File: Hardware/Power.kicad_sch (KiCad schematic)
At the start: 17 parts

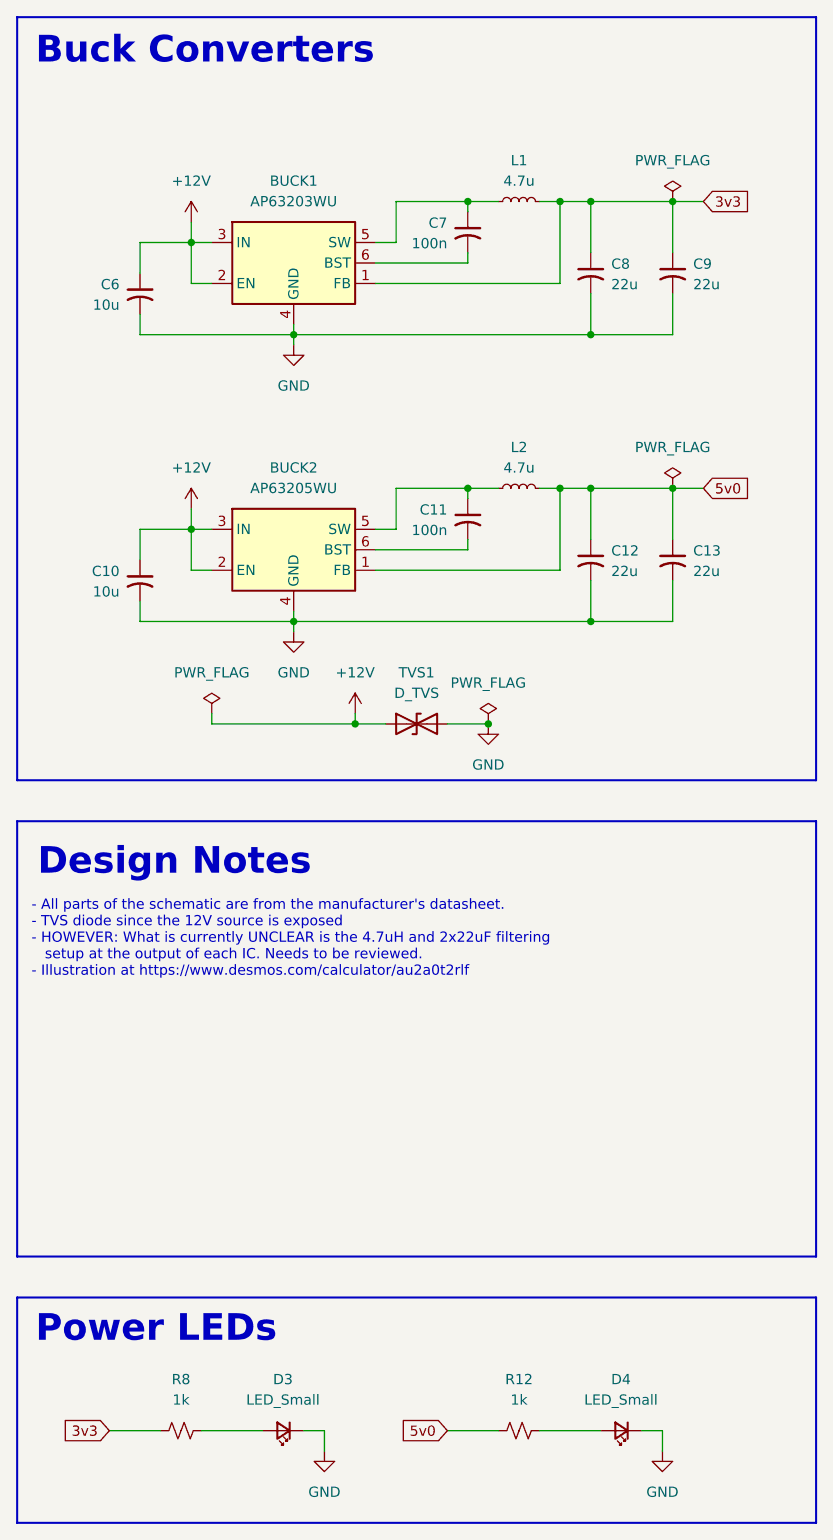
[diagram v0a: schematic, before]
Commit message: Fixed up the schematic a little, and did *most* footprint assigning
- Most footprints are assigned. Ones that arent either don't exist, or
  are out of stock at digikey and are thus not work making/adding.
- Details of next steps will be put into changelog soon
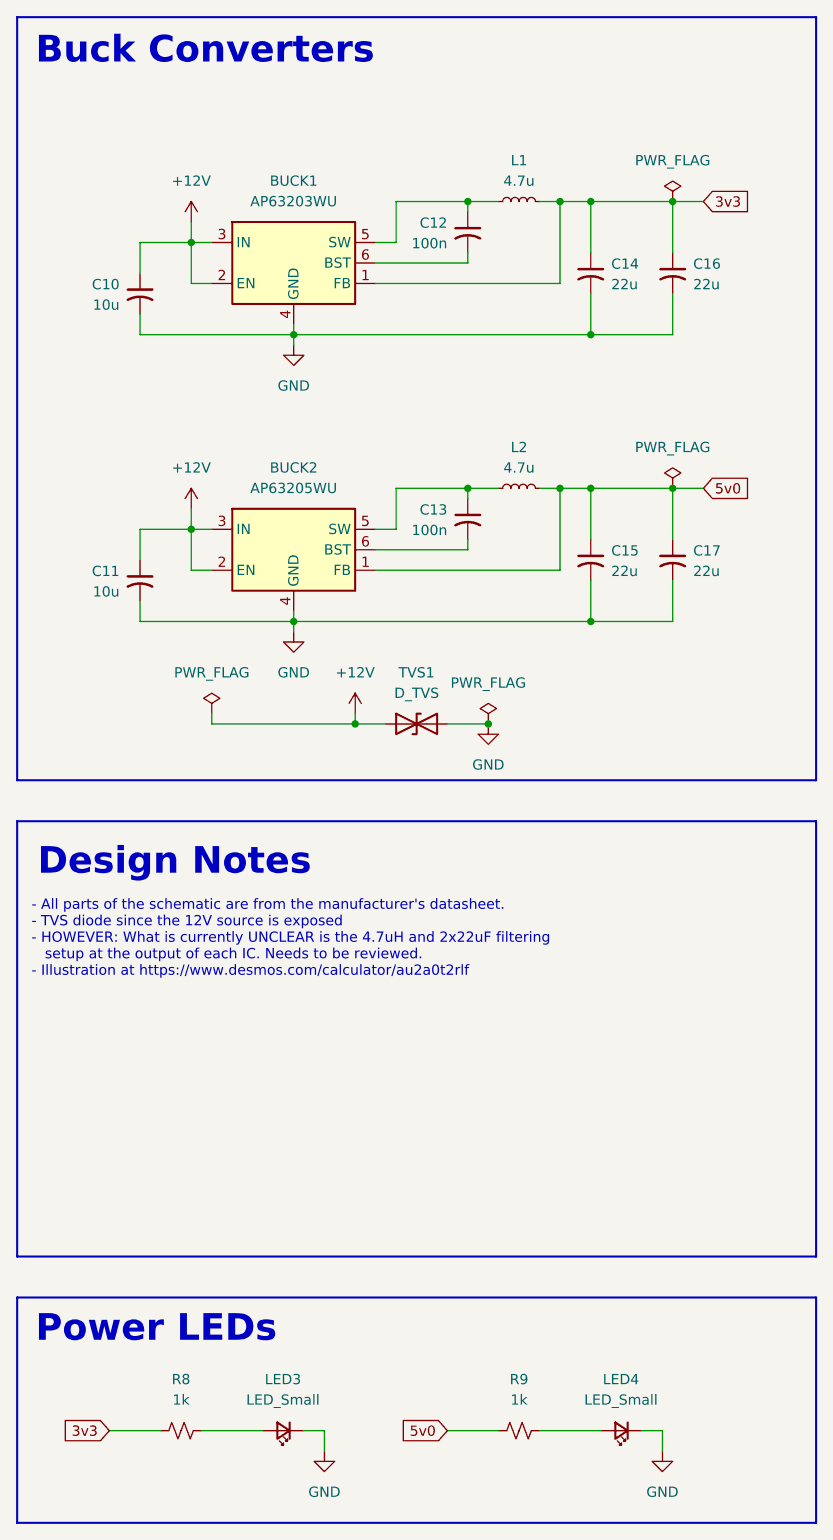
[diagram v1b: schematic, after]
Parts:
- C10: renamed from C6; footprint (none) -> Capacitor_SMD:C_0603_1608Metric_Pad1.08x0.95mm_HandSolder
- C11: renamed from C10; footprint (none) -> Capacitor_SMD:C_0603_1608Metric_Pad1.08x0.95mm_HandSolder
- C12: renamed from C7; footprint (none) -> Capacitor_SMD:C_0603_1608Metric_Pad1.08x0.95mm_HandSolder
- C13: renamed from C11; footprint (none) -> Capacitor_SMD:C_0603_1608Metric_Pad1.08x0.95mm_HandSolder
- C14: renamed from C8; footprint (none) -> Capacitor_SMD:CP_Elec_4x4.5
- C15: renamed from C12; footprint (none) -> Capacitor_SMD:CP_Elec_4x4.5
- C16: renamed from C9; footprint (none) -> Capacitor_SMD:CP_Elec_4x4.5
- C17: renamed from C13; footprint (none) -> Capacitor_SMD:CP_Elec_4x4.5
- L1, L2: footprint (none) -> Inductor_THT:L_Axial_L7.0mm_D3.3mm_P5.08mm_Vertical_Fastron_MICC
- LED3: renamed from D3; footprint (none) -> LED_SMD:LED_1206_3216Metric_Pad1.42x1.75mm_HandSolder
- LED4: renamed from D4; footprint (none) -> LED_SMD:LED_1206_3216Metric_Pad1.42x1.75mm_HandSolder
- R8: footprint (none) -> Resistor_SMD:R_0603_1608Metric_Pad0.98x0.95mm_HandSolder
- R9: renamed from R12; footprint (none) -> Resistor_SMD:R_0603_1608Metric_Pad0.98x0.95mm_HandSolder
- TVS1: footprint (none) -> Diode_SMD:D_SMA_Handsoldering
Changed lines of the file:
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@@
 		(on_board yes)
 		(dnp no)
-		(property "Reference" "C8"
+		(property "Reference" "C14"
 			(at 88.9 45.8469 0)
 			(effects
@@
 			)
 		)
-		(property "Footprint" ""
+		(property "Footprint" "Capacitor_SMD:CP_Elec_4x4.5"
 			(at 86.36 46.99 0)
 			(effects
@@
 			(project "CANIO-Board"
 				(path "/a11f98b2-3b09-4cf9-8535-19e509fe91b9/689b7a23-36b5-40a7-9bc7-70c150316ec6"
-					(reference "C8")
+					(reference "C14")
 					(unit 1)
 				)
@@
 		(dnp no)
 		(fields_autoplaced yes)
-		(property "Reference" "#PWR033"
+		(property "Reference" "#PWR04"
 			(at 36.83 44.45 0)
 			(effects
@@
 			(project ""
 				(path "/a11f98b2-3b09-4cf9-8535-19e509fe91b9/689b7a23-36b5-40a7-9bc7-70c150316ec6"
-					(reference "#PWR033")
+					(reference "#PWR04")
 					(unit 1)
 				)
@@
 		(on_board yes)
 		(dnp no)
-		(property "Reference" "C6"
+		(property "Reference" "C10"
 			(at 27.94 48.3869 0)
 			(effects
@@
 			)
 		)
-		(property "Footprint" ""
+		(property "Footprint" "Capacitor_SMD:C_0603_1608Metric_Pad1.08x0.95mm_HandSolder"
 			(at 30.48 49.53 0)
 			(effects
@@
 			(project "CANIO-Board"
 				(path "/a11f98b2-3b09-4cf9-8535-19e509fe91b9/689b7a23-36b5-40a7-9bc7-70c150316ec6"
-					(reference "C6")
+					(reference "C10")
 					(unit 1)
 				)
@@
 		(dnp no)
 		(fields_autoplaced yes)
-		(property "Reference" "R12"
+		(property "Reference" "R9"
 			(at 77.47 184.15 90)
 			(effects
@@
 			)
 		)
-		(property "Footprint" ""
+		(property "Footprint" "Resistor_SMD:R_0603_1608Metric_Pad0.98x0.95mm_HandSolder"
 			(at 77.47 190.5 0)
 			(effects
@@
 			(project "CANIO-Board"
 				(path "/a11f98b2-3b09-4cf9-8535-19e509fe91b9/689b7a23-36b5-40a7-9bc7-70c150316ec6"
-					(reference "R12")
+					(reference "R9")
 					(unit 1)
 				)
@@
 		(dnp no)
 		(fields_autoplaced yes)
-		(property "Reference" "#PWR011"
+		(property "Reference" "#PWR09"
 			(at 57.15 105.41 0)
 			(effects
@@
 			(project "CANIO-Board"
 				(path "/a11f98b2-3b09-4cf9-8535-19e509fe91b9/689b7a23-36b5-40a7-9bc7-70c150316ec6"
-					(reference "#PWR011")
+					(reference "#PWR09")
 					(unit 1)
 				)
@@
 		(dnp no)
 		(fields_autoplaced yes)
-		(property "Reference" "#FLG01"
+		(property "Reference" "#FLG03"
 			(at 96.52 36.195 0)
 			(effects
@@
 			(project ""
 				(path "/a11f98b2-3b09-4cf9-8535-19e509fe91b9/689b7a23-36b5-40a7-9bc7-70c150316ec6"
-					(reference "#FLG01")
+					(reference "#FLG03")
 					(unit 1)
 				)
@@
 		(dnp no)
 		(fields_autoplaced yes)
-		(property "Reference" "#PWR02"
+		(property "Reference" "#PWR07"
 			(at 49.53 97.79 0)
 			(effects
@@
 			(project "CANIO-Board"
 				(path "/a11f98b2-3b09-4cf9-8535-19e509fe91b9/689b7a23-36b5-40a7-9bc7-70c150316ec6"
-					(reference "#PWR02")
+					(reference "#PWR07")
 					(unit 1)
 				)
@@
 		(dnp no)
 		(fields_autoplaced yes)
-		(property "Reference" "#FLG04"
+		(property "Reference" "#FLG01"
 			(at 39.37 99.695 0)
 			(effects
@@
 			(project "CANIO-Board"
 				(path "/a11f98b2-3b09-4cf9-8535-19e509fe91b9/689b7a23-36b5-40a7-9bc7-70c150316ec6"
-					(reference "#FLG04")
+					(reference "#FLG01")
 					(unit 1)
 				)
@@
 		(dnp no)
 		(fields_autoplaced yes)
-		(property "Reference" "#FLG03"
+		(property "Reference" "#FLG02"
 			(at 73.66 100.965 0)
 			(effects
@@
 			(project "CANIO-Board"
 				(path "/a11f98b2-3b09-4cf9-8535-19e509fe91b9/689b7a23-36b5-40a7-9bc7-70c150316ec6"
-					(reference "#FLG03")
+					(reference "#FLG02")
 					(unit 1)
 				)
@@
 		(on_board yes)
 		(dnp no)
-		(property "Reference" "C10"
+		(property "Reference" "C11"
 			(at 27.94 83.9469 0)
 			(effects
@@
 			)
 		)
-		(property "Footprint" ""
+		(property "Footprint" "Capacitor_SMD:C_0603_1608Metric_Pad1.08x0.95mm_HandSolder"
 			(at 30.48 85.09 0)
 			(effects
@@
 			(project "CANIO-Board"
 				(path "/a11f98b2-3b09-4cf9-8535-19e509fe91b9/689b7a23-36b5-40a7-9bc7-70c150316ec6"
-					(reference "C10")
+					(reference "C11")
 					(unit 1)
 				)
@@
 		(dnp no)
 		(fields_autoplaced yes)
-		(property "Reference" "#FLG02"
+		(property "Reference" "#FLG04"
 			(at 96.52 71.755 0)
 			(effects
@@
 			(project "CANIO-Board"
 				(path "/a11f98b2-3b09-4cf9-8535-19e509fe91b9/689b7a23-36b5-40a7-9bc7-70c150316ec6"
-					(reference "#FLG02")
+					(reference "#FLG04")
 					(unit 1)
 				)
@@
 			)
 		)
-		(property "Footprint" ""
+		(property "Footprint" "Inductor_THT:L_Axial_L7.0mm_D3.3mm_P5.08mm_Vertical_Fastron_MICC"
 			(at 77.47 73.66 0)
 			(effects
@@
 			)
 		)
-		(property "Footprint" ""
+		(property "Footprint" "Inductor_THT:L_Axial_L7.0mm_D3.3mm_P5.08mm_Vertical_Fastron_MICC"
 			(at 77.47 38.1 0)
 			(effects
@@
 		(on_board yes)
 		(dnp no)
-		(property "Reference" "C9"
+		(property "Reference" "C16"
 			(at 99.06 45.8469 0)
 			(effects
@@
 			)
 		)
-		(property "Footprint" ""
+		(property "Footprint" "Capacitor_SMD:CP_Elec_4x4.5"
 			(at 96.52 46.99 0)
 			(effects
@@
 			(project "CANIO-Board"
 				(path "/a11f98b2-3b09-4cf9-8535-19e509fe91b9/689b7a23-36b5-40a7-9bc7-70c150316ec6"
-					(reference "C9")
+					(reference "C16")
 					(unit 1)
 				)
@@
 		(dnp no)
 		(fields_autoplaced yes)
-		(property "Reference" "#PWR01"
+		(property "Reference" "#PWR05"
 			(at 36.83 80.01 0)
 			(effects
@@
 			(project "CANIO-Board"
 				(path "/a11f98b2-3b09-4cf9-8535-19e509fe91b9/689b7a23-36b5-40a7-9bc7-70c150316ec6"
-					(reference "#PWR01")
+					(reference "#PWR05")
 					(unit 1)
 				)
@@
 		(dnp no)
 		(fields_autoplaced yes)
-		(property "Reference" "D3"
+		(property "Reference" "LED3"
 			(at 48.1965 184.15 0)
 			(effects
@@
 			)
 		)
-		(property "Footprint" ""
+		(property "Footprint" "LED_SMD:LED_1206_3216Metric_Pad1.42x1.75mm_HandSolder"
 			(at 48.26 190.5 90)
 			(effects
@@
 			(project ""
 				(path "/a11f98b2-3b09-4cf9-8535-19e509fe91b9/689b7a23-36b5-40a7-9bc7-70c150316ec6"
-					(reference "D3")
+					(reference "LED3")
 					(unit 1)
 				)
@@
 		(dnp no)
 		(fields_autoplaced yes)
-		(property "Reference" "D4"
+		(property "Reference" "LED4"
 			(at 90.1065 184.15 0)
 			(effects
@@
 			)
 		)
-		(property "Footprint" ""
+		(property "Footprint" "LED_SMD:LED_1206_3216Metric_Pad1.42x1.75mm_HandSolder"
 			(at 90.17 190.5 90)
 			(effects
@@
 			(project "CANIO-Board"
 				(path "/a11f98b2-3b09-4cf9-8535-19e509fe91b9/689b7a23-36b5-40a7-9bc7-70c150316ec6"
-					(reference "D4")
+					(reference "LED4")
 					(unit 1)
 				)
@@
 		(dnp no)
 		(fields_autoplaced yes)
-		(property "Reference" "#PWR012"
+		(property "Reference" "#PWR010"
 			(at 73.66 109.22 0)
 			(effects
@@
 			(project "CANIO-Board"
 				(path "/a11f98b2-3b09-4cf9-8535-19e509fe91b9/689b7a23-36b5-40a7-9bc7-70c150316ec6"
-					(reference "#PWR012")
+					(reference "#PWR010")
 					(unit 1)
 				)
@@
 		(on_board yes)
 		(dnp no)
-		(property "Reference" "C7"
+		(property "Reference" "C12"
 			(at 68.58 40.7669 0)
 			(effects
@@
 			)
 		)
-		(property "Footprint" ""
+		(property "Footprint" "Capacitor_SMD:C_0603_1608Metric_Pad1.08x0.95mm_HandSolder"
 			(at 71.12 41.91 0)
 			(effects
@@
 			(project "CANIO-Board"
 				(path "/a11f98b2-3b09-4cf9-8535-19e509fe91b9/689b7a23-36b5-40a7-9bc7-70c150316ec6"
-					(reference "C7")
+					(reference "C12")
 					(unit 1)
 				)
@@
 		(on_board yes)
 		(dnp no)
-		(property "Reference" "C11"
+		(property "Reference" "C13"
 			(at 68.58 76.3269 0)
 			(effects
@@
 			)
 		)
-		(property "Footprint" ""
+		(property "Footprint" "Capacitor_SMD:C_0603_1608Metric_Pad1.08x0.95mm_HandSolder"
 			(at 71.12 77.47 0)
 			(effects
@@
 			(project "CANIO-Board"
 				(path "/a11f98b2-3b09-4cf9-8535-19e509fe91b9/689b7a23-36b5-40a7-9bc7-70c150316ec6"
-					(reference "C11")
+					(reference "C13")
 					(unit 1)
 				)
@@
 		(dnp no)
 		(fields_autoplaced yes)
-		(property "Reference" "#PWR014"
+		(property "Reference" "#PWR08"
 			(at 53.34 199.39 0)
 			(effects
@@
 			(project ""
 				(path "/a11f98b2-3b09-4cf9-8535-19e509fe91b9/689b7a23-36b5-40a7-9bc7-70c150316ec6"
-					(reference "#PWR014")
+					(reference "#PWR08")
 					(unit 1)
 				)
@@
 		(dnp no)
 		(fields_autoplaced yes)
-		(property "Reference" "#PWR032"
+		(property "Reference" "#PWR06"
 			(at 49.53 62.23 0)
 			(effects
@@
 			(project ""
 				(path "/a11f98b2-3b09-4cf9-8535-19e509fe91b9/689b7a23-36b5-40a7-9bc7-70c150316ec6"
-					(reference "#PWR032")
+					(reference "#PWR06")
 					(unit 1)
 				)
@@
 			)
 		)
-		(property "Footprint" ""
+		(property "Footprint" "Resistor_SMD:R_0603_1608Metric_Pad0.98x0.95mm_HandSolder"
 			(at 35.56 190.5 0)
 			(effects
@@
 			)
 		)
-		(property "Footprint" ""
+		(property "Footprint" "Diode_SMD:D_SMA_Handsoldering"
 			(at 64.77 102.87 0)
 			(effects
@@
 		(on_board yes)
 		(dnp no)
-		(property "Reference" "C13"
+		(property "Reference" "C17"
 			(at 99.06 81.4069 0)
 			(effects
@@
 			)
 		)
-		(property "Footprint" ""
+		(property "Footprint" "Capacitor_SMD:CP_Elec_4x4.5"
 			(at 96.52 82.55 0)
 			(effects
@@
 			(project "CANIO-Board"
 				(path "/a11f98b2-3b09-4cf9-8535-19e509fe91b9/689b7a23-36b5-40a7-9bc7-70c150316ec6"
-					(reference "C13")
+					(reference "C17")
 					(unit 1)
 				)
@@
 		(on_board yes)
 		(dnp no)
-		(property "Reference" "C12"
+		(property "Reference" "C15"
 			(at 88.9 81.4069 0)
 			(effects
@@
 			)
 		)
-		(property "Footprint" ""
+		(property "Footprint" "Capacitor_SMD:CP_Elec_4x4.5"
 			(at 86.36 82.55 0)
 			(effects
@@
 			(project "CANIO-Board"
 				(path "/a11f98b2-3b09-4cf9-8535-19e509fe91b9/689b7a23-36b5-40a7-9bc7-70c150316ec6"
-					(reference "C12")
+					(reference "C15")
 					(unit 1)
 				)
@@
 		(dnp no)
 		(fields_autoplaced yes)
-		(property "Reference" "#PWR018"
+		(property "Reference" "#PWR011"
 			(at 95.25 199.39 0)
 			(effects
@@
 			(project "CANIO-Board"
 				(path "/a11f98b2-3b09-4cf9-8535-19e509fe91b9/689b7a23-36b5-40a7-9bc7-70c150316ec6"
-					(reference "#PWR018")
-					(unit 1)
-				)
+					(reference "#PWR011")
+					(unit 1)
+				)
